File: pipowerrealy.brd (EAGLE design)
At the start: 61 x 27.9 mm, 8 parts, among them K1 RR1A, P1 ZX62D-B-5P8, P2 480-37-1000

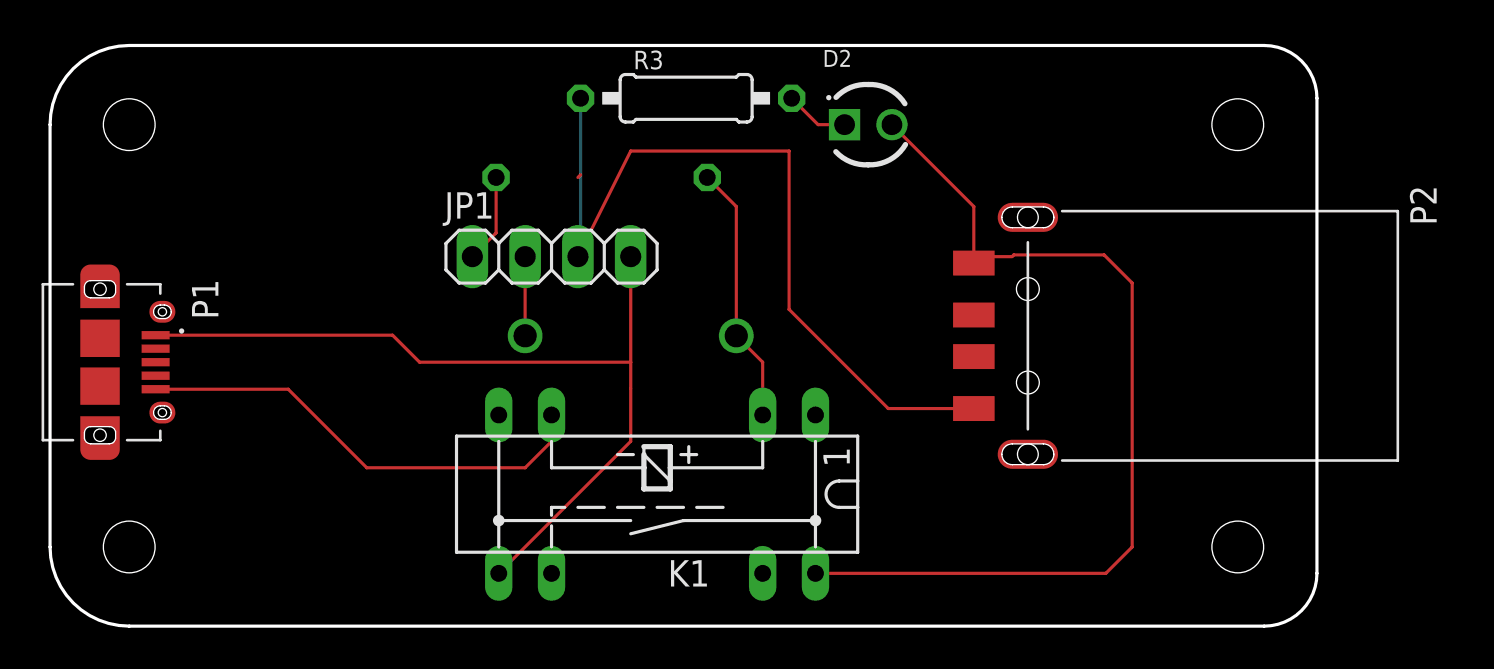
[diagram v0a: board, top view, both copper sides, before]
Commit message: Shrank board. Made a problem for Vccin vs vccout.
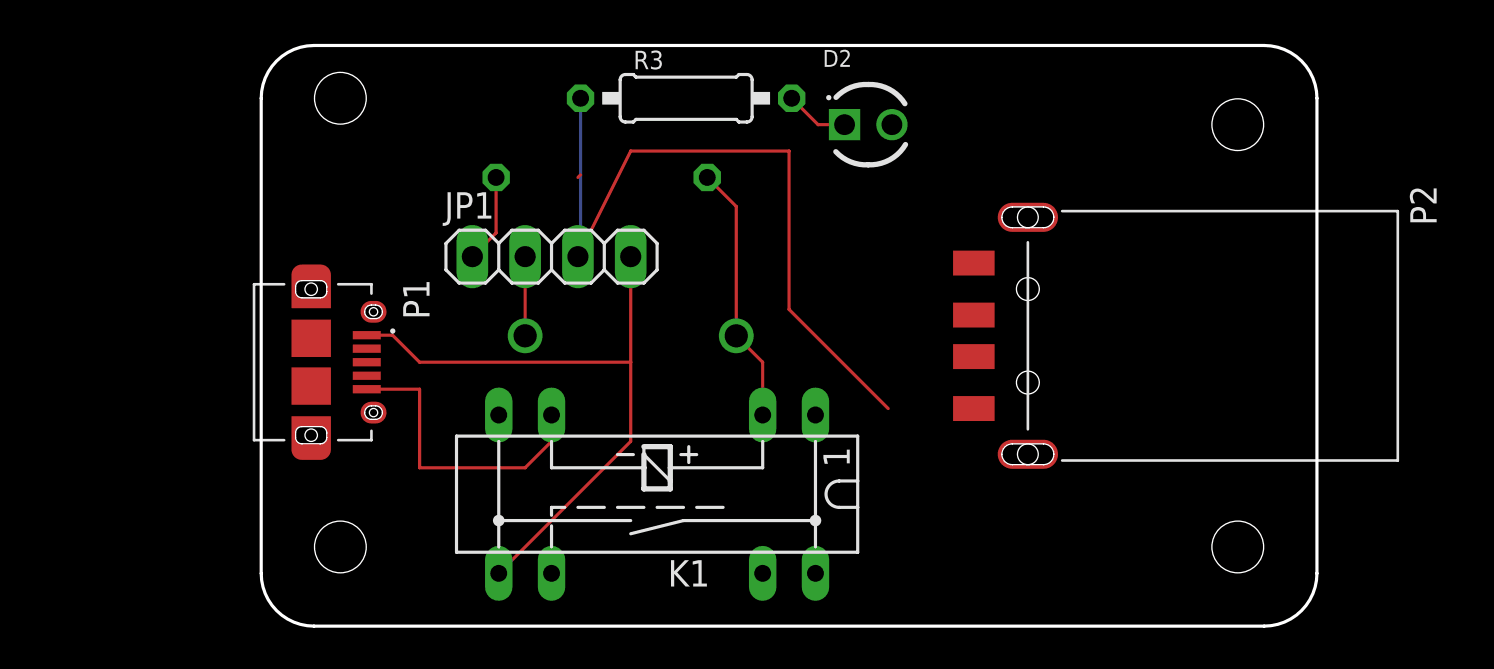
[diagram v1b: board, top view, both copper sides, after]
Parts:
- moved P1 10.2 mm to (16.5, 49.5)
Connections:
- removed net N$3: K1.6, P1.5
- removed net N$5: D2.A, K1.14, P2.1
- net GND: now also K1.14, P1.5
- net VCC: now also D2.A, P2.1
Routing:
- net N$5: track 45.0 -> 0.00 mm
- net N$3: track 22.4 -> 0.00 mm
- net VCC: track 41.3 -> 31.1 mm
- net GND: track 39.8 -> 48.9 mm
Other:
- board size 61 x 27.9 mm -> 50.8 x 27.9 mm
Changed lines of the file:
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@@
 <fusionsync huburn="a.cGVyc29uYWw6dWUyOWU0ODVi" projecturn="a.cGVyc29uYWw6dWUyOWU0ODViIzIwMTgwMzA2MTIxMzA5MTUx" f3durn="urn:adsk.wipprod:dm.lineage:fopLNIwJTTSRYJuhp4E_3g" pcbguid="8ab28e49-b7c2-4085-baea-5a720d3ce358" lastpulledtime="" lastsyncedchangeguid="2516de99-68e5-59f1-5365-ec519843f962"/>
 <plain>
-<wire x1="5.08" y1="64.77" x2="59.69" y2="64.77" width="0.1524" layer="20"/>
+<wire x1="13.97" y1="64.77" x2="59.69" y2="64.77" width="0.1524" layer="20"/>
 <wire x1="59.69" y1="64.77" x2="62.23" y2="62.23" width="0.1524" layer="20" curve="-90"/>
 <wire x1="62.23" y1="62.23" x2="62.23" y2="39.37" width="0.1524" layer="20"/>
 <wire x1="62.23" y1="39.37" x2="59.69" y2="36.83" width="0.1524" layer="20" curve="-90"/>
-<wire x1="59.69" y1="36.83" x2="5.08" y2="36.83" width="0.1524" layer="20"/>
-<wire x1="5.08" y1="36.83" x2="1.27" y2="40.64" width="0.1524" layer="20" curve="-90"/>
-<wire x1="1.27" y1="40.64" x2="1.27" y2="60.96" width="0.1524" layer="20"/>
-<wire x1="1.27" y1="60.96" x2="5.08" y2="64.77" width="0.1524" layer="20" curve="-90"/>
+<wire x1="59.69" y1="36.83" x2="13.97" y2="36.83" width="0.1524" layer="20"/>
+<wire x1="13.97" y1="36.83" x2="11.43" y2="39.37" width="0.1524" layer="20" curve="-90"/>
+<wire x1="11.43" y1="39.37" x2="11.43" y2="62.23" width="0.1524" layer="20"/>
+<wire x1="11.43" y1="62.23" x2="13.97" y2="64.77" width="0.1524" layer="20" curve="-90"/>
 <hole x="58.42" y="60.96" drill="2.4892"/>
 <hole x="58.42" y="40.64" drill="2.4892"/>
-<hole x="5.08" y="60.96" drill="2.4892"/>
-<hole x="5.08" y="40.64" drill="2.4892"/>
+<hole x="15.24" y="62.23" drill="2.4892"/>
+<hole x="15.24" y="40.64" drill="2.4892"/>
 </plain>
 <attributes>
@@
 <attribute name="OC_NEWARK" value="unknown" x="30.48" y="43.18" size="1.778" layer="27" rot="R180" display="off"/>
 </element>
-<element name="P1" library="Common-Parts-Library-Eagle" package="HRS_ZX62D-B-5P8" value="ZX62D-B-5P8" x="6.35" y="49.53" rot="R270">
-<attribute name="MANUFACTURER" value="Hirose" x="6.35" y="49.53" size="1.778" layer="27" rot="R270" display="off"/>
+<element name="P1" library="Common-Parts-Library-Eagle" package="HRS_ZX62D-B-5P8" value="ZX62D-B-5P8" x="16.51" y="49.53" rot="R270">
+<attribute name="MANUFACTURER" value="Hirose" x="16.51" y="49.53" size="1.778" layer="27" rot="R270" display="off"/>
 </element>
 <element name="P2" library="Common-Parts-Library-Eagle" package="MOLEX_480-37-1000" value="480-37-1000" x="45.72" y="50.8" rot="R270">
@@
 <contactref element="JP1" pad="4"/>
 <wire x1="22.86" y1="39.37" x2="29.21" y2="45.72" width="0.1524" layer="1"/>
-<wire x1="29.21" y1="45.72" x2="29.21" y2="48.26" width="0.1524" layer="1"/>
-<wire x1="29.21" y1="48.26" x2="29.21" y2="49.53" width="0.1524" layer="1"/>
+<wire x1="29.21" y1="45.72" x2="29.21" y2="49.53" width="0.1524" layer="1"/>
 <wire x1="29.21" y1="49.53" x2="29.21" y2="54.61" width="0.1524" layer="1"/>
-<wire x1="6.35" y1="50.83" x2="17.75" y2="50.83" width="0.1524" layer="1"/>
 <wire x1="19.05" y1="49.53" x2="29.21" y2="49.53" width="0.1524" layer="1"/>
 <wire x1="17.75" y1="50.83" x2="19.05" y2="49.53" width="0.1524" layer="1"/>
+<contactref element="D2" pad="A"/>
+<contactref element="P2" pad="1"/>
+<wire x1="16.51" y1="50.83" x2="17.75" y2="50.83" width="0.1524" layer="1"/>
+<wire x1="45.72" y1="54.3" x2="41.78" y2="60.96" width="0" layer="19" extent="1-1"/>
+<wire x1="29.21" y1="54.61" x2="41.78" y2="60.96" width="0" layer="19" extent="1-1"/>
 </signal>
 <signal name="GND">
 <contactref element="JP1" pad="3"/>
-<contactref element="P2" pad="4"/>
 <contactref element="R3" pad="1"/>
 <wire x1="26.797" y1="58.547" x2="26.67" y2="58.42" width="0.1524" layer="1"/>
@@
 <wire x1="29.21" y1="59.69" x2="36.83" y2="59.69" width="0.1524" layer="1"/>
 <wire x1="36.83" y1="59.69" x2="36.83" y2="52.07" width="0.1524" layer="1"/>
-<wire x1="41.6" y1="47.3" x2="45.72" y2="47.3" width="0.1524" layer="1"/>
 <wire x1="36.83" y1="52.07" x2="41.6" y2="47.3" width="0.1524" layer="1"/>
 <wire x1="26.67" y1="54.61" x2="26.797" y2="54.737" width="0.1524" layer="16"/>
 <wire x1="26.797" y1="54.737" x2="26.797" y2="62.23" width="0.1524" layer="16"/>
-<wire x1="29.21" y1="59.69" x2="26.797" y2="58.547" width="0" layer="19" extent="1-1"/>
+<contactref element="K1" pad="14"/>
+<contactref element="P1" pad="5"/>
+<wire x1="24.13" y1="44.45" x2="25.4" y2="45.72" width="0.1524" layer="1"/>
+<contactref element="P2" pad="4"/>
+<wire x1="16.51" y1="48.23" x2="19.05" y2="48.23" width="0.1524" layer="1"/>
+<wire x1="19.05" y1="48.23" x2="19.05" y2="44.45" width="0.1524" layer="1"/>
+<wire x1="19.05" y1="44.45" x2="24.13" y2="44.45" width="0.1524" layer="1"/>
+<wire x1="41.6" y1="47.3" x2="45.72" y2="47.3" width="0" layer="19" extent="1-1"/>
+<wire x1="26.797" y1="58.547" x2="29.21" y2="59.69" width="0" layer="19" extent="1-1"/>
+<wire x1="38.1" y1="39.37" x2="41.6" y2="47.3" width="0" layer="19" extent="1-1"/>
+<wire x1="25.4" y1="45.72" x2="26.67" y2="54.61" width="0" layer="19" extent="1-1"/>
 </signal>
 <signal name="N$2">
@@
 <contactref element="JP1" pad="2"/>
 <wire x1="24.13" y1="54.61" x2="24.13" y2="50.8" width="0.1524" layer="1"/>
-</signal>
-<signal name="N$3">
-<contactref element="P1" pad="5"/>
-<contactref element="K1" pad="6"/>
-<wire x1="6.35" y1="48.23" x2="12.73" y2="48.23" width="0.1524" layer="1"/>
-<wire x1="12.73" y1="48.23" x2="16.51" y2="44.45" width="0.1524" layer="1"/>
-<wire x1="16.51" y1="44.45" x2="24.13" y2="44.45" width="0.1524" layer="1"/>
-<wire x1="24.13" y1="44.45" x2="25.4" y2="45.72" width="0.1524" layer="1"/>
-<wire x1="25.4" y1="45.72" x2="25.4" y2="46.99" width="0.1524" layer="1"/>
 </signal>
 <signal name="N$4">
@@
 <wire x1="38.227" y1="60.96" x2="39.5" y2="60.96" width="0.1524" layer="1"/>
 </signal>
-<signal name="N$5">
-<contactref element="P2" pad="1"/>
-<contactref element="D2" pad="A"/>
-<contactref element="K1" pad="14"/>
-<wire x1="41.78" y1="60.96" x2="45.72" y2="57.02" width="0.1524" layer="1"/>
-<wire x1="45.72" y1="57.02" x2="45.72" y2="54.61" width="0.1524" layer="1"/>
-<wire x1="45.72" y1="54.61" x2="45.72" y2="54.3" width="0.1524" layer="1"/>
-<wire x1="38.1" y1="39.37" x2="52.07" y2="39.37" width="0.1524" layer="1"/>
-<wire x1="52.07" y1="39.37" x2="53.34" y2="40.64" width="0.1524" layer="1"/>
-<wire x1="53.34" y1="40.64" x2="53.34" y2="53.34" width="0.1524" layer="1"/>
-<wire x1="47.639775" y1="54.6922" x2="47.557575" y2="54.61" width="0.1524" layer="1"/>
-<wire x1="47.557575" y1="54.61" x2="45.72" y2="54.61" width="0.1524" layer="1"/>
-<wire x1="53.34" y1="53.34" x2="51.9878" y2="54.6922" width="0.1524" layer="1"/>
-<wire x1="51.9878" y1="54.6922" x2="47.639775" y2="54.6922" width="0.1524" layer="1"/>
-</signal>
 <signal name="N$6">
